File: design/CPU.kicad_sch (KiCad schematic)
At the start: 8 parts, among them J7 Conn_02x32_Odd_Even, U10 MC68010P, Y4 SG-5032CAN 10MHz

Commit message: Fix all R/C part numbers: switch to JLCPCB basic parts, correct footprints
- Replace all non-basic LCSC numbers with JLCPCB basic equivalents (no
  extended part setup fees): Samsung MLCCs for caps, UNI-ROYAL 0805W8F
  series for resistors
- Fix C49 footprint: 1210 → 1206 to match Samsung CL31A476MPHNNNE
- Correct previously wrong LCSC numbers (C17512→C17513, C17515→C17673,
  C135808→C96123) and missing R17 part numbers
- Update all Mouser numbers to match the LCSC manufacturer throughout
- Standardise all resistor footprints to HandSolder pad variant
- Update datasheets/INDEX.md with verified basic part table

Co-Authored-By: Claude Sonnet 4.6 <noreply@anthropic.com>
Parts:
- C31: LCSC C89827 -> C15850; Mouser 603-CC0805KKX5R7BB106 -> 187-CL21A106KAYNNNE
- R19: LCSC C84376 -> C17414; Mouser 603-RC0805FR-0710KL -> 0805W8F1002T5E
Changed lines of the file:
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@@
 			)
 		)
-		(property "Mouser" "603-CC0805KKX5R7BB106"
+		(property "Mouser" "187-CL21A106KAYNNNE"
 			(at 114.3 26.67 0)
 			(hide yes)
@@
 			)
 		)
-		(property "LCSC" "C89827"
+		(property "LCSC" "C15850"
 			(at 114.3 26.67 0)
 			(hide yes)
@@
 			)
 		)
-		(property "Mouser" "603-RC0805FR-0710KL"
+		(property "Mouser" "0805W8F1002T5E "
 			(at 167.64 41.91 0)
 			(hide yes)
@@
 			)
 		)
-		(property "LCSC" "C84376"
+		(property "LCSC" "C17414"
 			(at 167.64 41.91 0)
 			(hide yes)

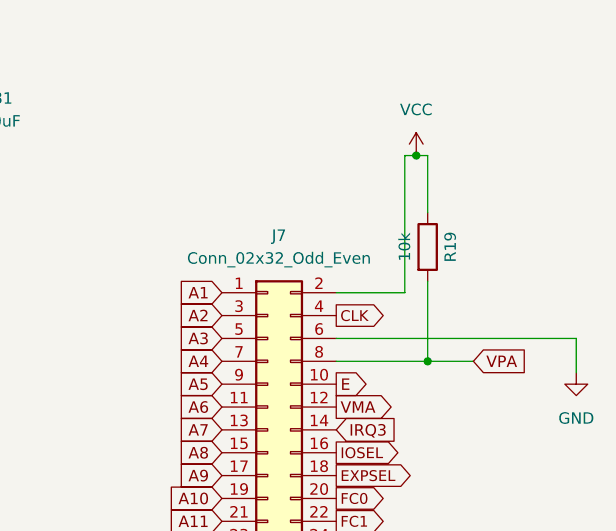
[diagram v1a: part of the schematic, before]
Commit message: Fix even/odd memory bus wiring and route PCB
- Connect U15 (even ROM) and U17 (even RAM) data pins to D8-D15 instead
  of D0-D7: upper byte was completely unconnected, causing half-garbage
  reads and lost writes on all 16-bit accesses
- Reduce R32/R33 LED resistors from 4.7k to 1k (MCP2221A GPIO is 3.3V,
  4.7k gave only 0.26mA — too dim)
- Initial PCB layout and routing

Co-Authored-By: Claude Sonnet 4.6 <noreply@anthropic.com>
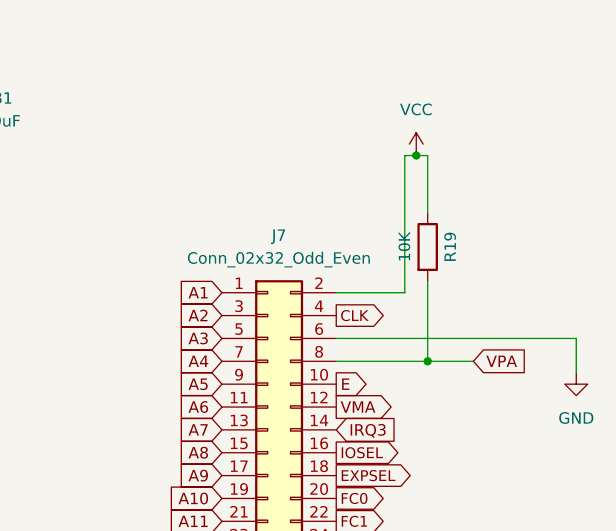
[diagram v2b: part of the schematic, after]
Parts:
- R19: value 10k -> 10K
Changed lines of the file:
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@@
 			)
 		)
-		(property "Value" "10k"
+		(property "Value" "10K"
 			(at 165.1 41.91 90)
 			(show_name no)

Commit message: Update KiCad design files and add fabrication outputs
Schematic and PCB updates including component renumbering (ICs, passives,
LEDs, oscillators). Add JLCPCB fabrication toolkit settings and v1
production outputs (gerbers zip, IPC netlist).

Co-Authored-By: Claude Sonnet 4.6 <noreply@anthropic.com>
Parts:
- renumbered C50 to C1, C43 to C2, C44 to C3, C31 to C4, R19 to R1, U10 to U1, Y4 to Y1
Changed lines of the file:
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@@
 		(dnp no)
 		(fields_autoplaced yes)
-		(property "Reference" "Y4"
+		(property "Reference" "Y1"
 			(at 113.03 109.1498 0)
 			(show_name no)
@@
 			(project "Simple010"
 				(path "/4f37455c-e998-4ed3-8493-a94956af64c1/2907fc67-7e28-48cc-93ca-028c1d99c5a1"
-					(reference "Y4")
+					(reference "Y1")
 					(unit 1)
 				)
@@
 		(in_pos_files yes)
 		(dnp no)
-		(property "Reference" "C50"
+		(property "Reference" "C1"
 			(at 83.82 26.67 90)
 			(show_name no)
@@
 			(project "Simple010"
 				(path "/4f37455c-e998-4ed3-8493-a94956af64c1/2907fc67-7e28-48cc-93ca-028c1d99c5a1"
-					(reference "C50")
+					(reference "C1")
 					(unit 1)
 				)
@@
 		(in_pos_files yes)
 		(dnp no)
-		(property "Reference" "C43"
+		(property "Reference" "C2"
 			(at 95.25 26.67 90)
 			(show_name no)
@@
 			(project "Simple010"
 				(path "/4f37455c-e998-4ed3-8493-a94956af64c1/2907fc67-7e28-48cc-93ca-028c1d99c5a1"
-					(reference "C43")
+					(reference "C2")
 					(unit 1)
 				)
@@
 		(in_pos_files yes)
 		(dnp no)
-		(property "Reference" "C44"
+		(property "Reference" "C3"
 			(at 107.95 26.67 90)
 			(show_name no)
@@
 			(project "Simple010"
 				(path "/4f37455c-e998-4ed3-8493-a94956af64c1/2907fc67-7e28-48cc-93ca-028c1d99c5a1"
-					(reference "C44")
+					(reference "C3")
 					(unit 1)
 				)
@@
 		(dnp no)
 		(fields_autoplaced yes)
-		(property "Reference" "C31"
+		(property "Reference" "C4"
 			(at 118.11 25.3999 0)
 			(show_name no)
@@
 			(project "Simple010"
 				(path "/4f37455c-e998-4ed3-8493-a94956af64c1/2907fc67-7e28-48cc-93ca-028c1d99c5a1"
-					(reference "C31")
+					(reference "C4")
 					(unit 1)
 				)
@@
 		(dnp no)
 		(fields_autoplaced yes)
-		(property "Reference" "U10"
+		(property "Reference" "U1"
 			(at 60.5633 39.37 0)
 			(show_name no)
@@
 			(project "Simple010"
 				(path "/4f37455c-e998-4ed3-8493-a94956af64c1/2907fc67-7e28-48cc-93ca-028c1d99c5a1"
-					(reference "U10")
+					(reference "U1")
 					(unit 1)
 				)
@@
 		(in_pos_files yes)
 		(dnp no)
-		(property "Reference" "R19"
+		(property "Reference" "R1"
 			(at 170.18 41.91 90)
 			(show_name no)
@@
 			(project "Simple010"
 				(path "/4f37455c-e998-4ed3-8493-a94956af64c1/2907fc67-7e28-48cc-93ca-028c1d99c5a1"
-					(reference "R19")
-					(unit 1)
-				)
+					(reference "R1")
+					(unit 1)
+				)
